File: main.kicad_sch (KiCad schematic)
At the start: 56 parts, among them IC11 BK4802P, IC12 PIC12LF1501-IP, IC14 PIC16F1503-ISL, J11 Conn_01x03, J12 Conn_01x06, J13 Conn_01x03, J14 Conn_01x03, J15 Conn_01x03, J19 Conn_Coaxial, Q11 2N7000, Q12 2N7000, Q13 2N7000, Q14 2N7000, Q15 2N7000, SW11 SW_SPDT, SW12 SW_Push, SW13 SW_Push, U11 LM2936-3.0_TO92, U12 LM2936-3.0, U13 LM2936-3.0, X11 Crystal

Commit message: 部品定数を入力　ただし未評価
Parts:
- C14: value 15p -> 22p
- C19: value 15p -> 27p
- C20: value 10u -> 470u
- C21: value 100p -> 1000p
- C30: value 0.1u -> 1u
- D11: value 1N4002 -> 1N4007
- IC12: value PIC12LF1501-IP -> PIC12F1501-I/P; now left out of the parts list
- IC14: value PIC16F1503-ISL -> PIC16F1503T-I/SL
- R13: value 1k -> 4.7k
- R16: value 1k -> 10
- U11: value LM2936-3.0_TO92 -> LP2950L-33-T92-K; now left out of the parts list
- U12: value LM2936-3.0 -> NJM2391DL1-33
- U13: value LM2936-3.0 -> LM2940T-3.3; now left out of the parts list
- X11: value Crystal -> 21.25M
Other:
- note added: "12Vの場合はレギュレータの放熱に注意 3.3V供給とする場合はU11でジャンパ"
- note added: "BAND"
- note added: "CAUTION: PCB mistake"
- note added: "DC IN"
- note added: "MIC"
- note added: "NM"
- note added: "PICKIT"
- note added: "PICkitからの電源で動かす場合 電源供給は3.3Vなので注意"
- note added: "PTT"
- note added: "R17はカイロミス 本来は3.3Vラインの切り離し用"
- note added: "SOPタイプのPICを使う前提 書き込みはコネクタにPICkitを接続して行う DIPを使う場合はPICkitのコネクタは実装できない"
- note added: "SPK"
- note added: "シリーズに抵抗を入れないと電源が厳しい"
- note added: "スケルチはコマンド制御不可なのでボリュームにすべき"
- note added: "ダイオードスイッチ用"
- note added: "ピン配置を間違えているので改造が必要"
- note added: "ミス：1/6Wパターン"
- note added: "レギュレータは使うたいものを実装 TO-92タイプは消費電流に注意 （スピーカ駆動は不可）"
- note added: "無線部分だけ切り離す場合に使う"
- note added: "逓倍数が大きいので周波数を合わせないと誤差が大きい"
- note added: "電源確認後に実装"
- company: (none) -> JK1MLY / PRUG
- title: (none) -> FM QRP TRCV

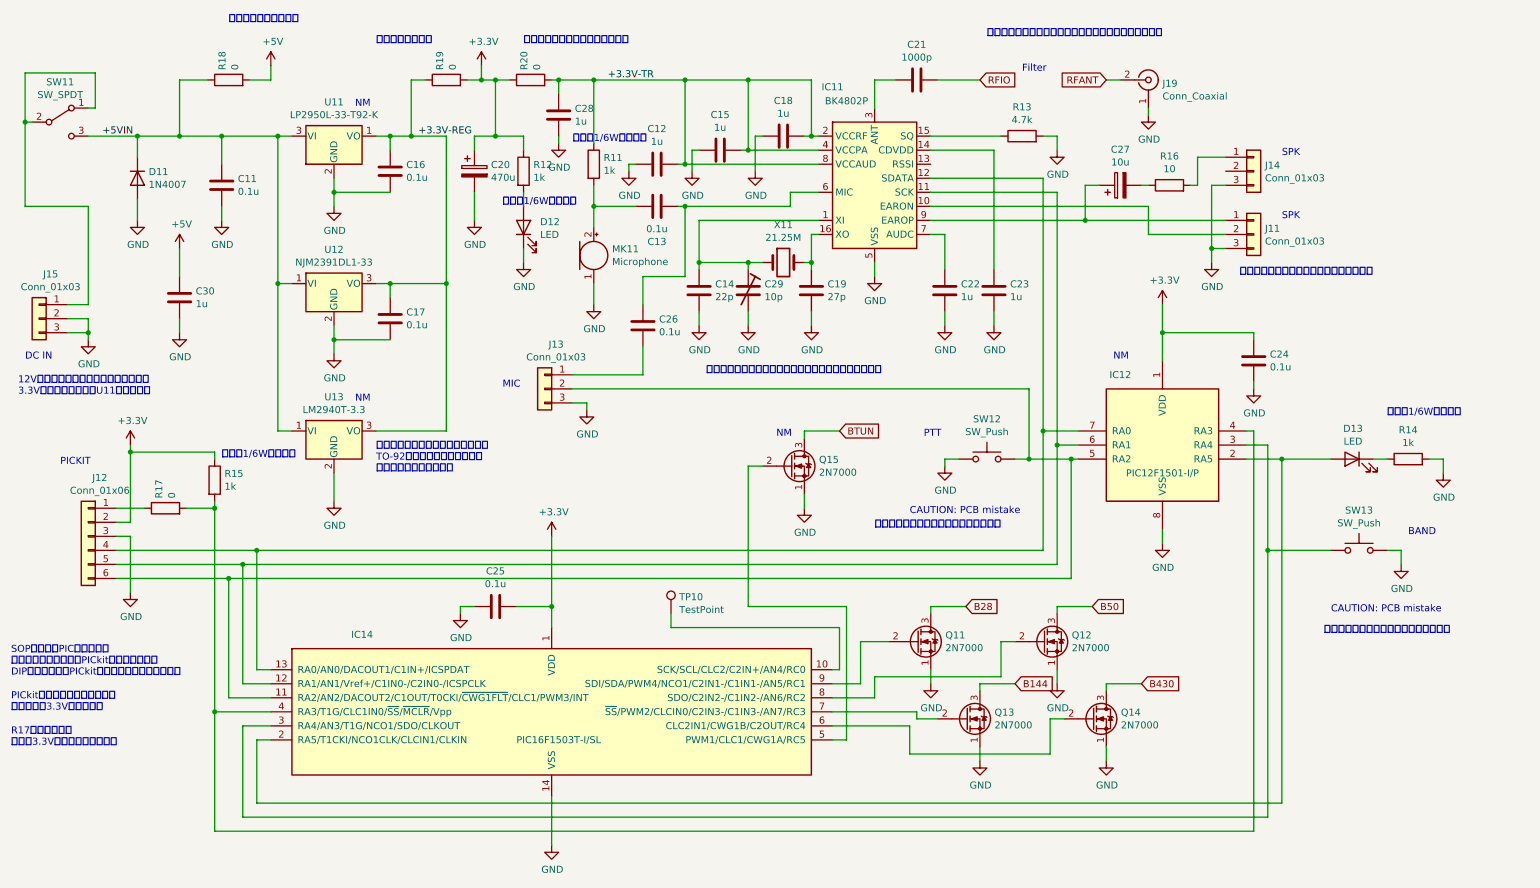
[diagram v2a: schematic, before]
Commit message: Add files via upload
フィルタ回路変更とジャンパクリーン
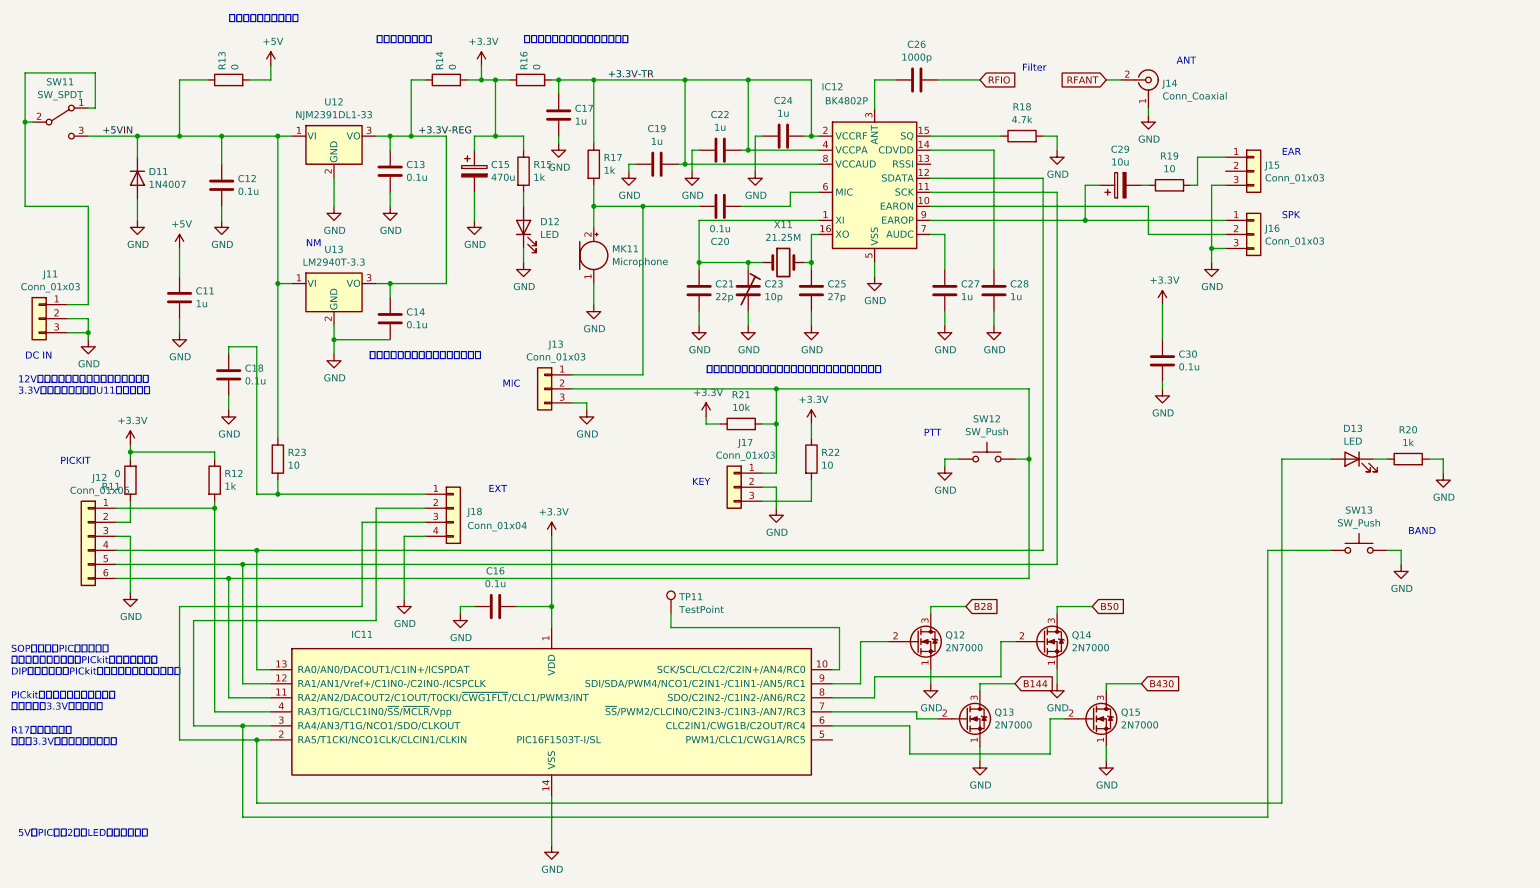
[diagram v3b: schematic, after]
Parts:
- removed C26: 0.1u, Capacitor_THT:C_Disc_D3.4mm_W2.1mm_P2.50mm, symbol Device:C
- removed IC12: PIC12F1501-I/P, digikey-footprints:DIP-8_W7.62mm, symbol MCU_Microchip_PIC12:PIC12LF1501-IP
- removed Q15: 2N7000, Package_TO_SOT_THT:TO-92_Inline_Wide, symbol Transistor_FET:2N7000
- removed U11: LP2950L-33-T92-K, Package_TO_SOT_THT:TO-92_Inline_Wide, symbol Regulator_Linear:LM2936-3.0_TO92
- added C18: 0.1u, Capacitor_THT:C_Disc_D3.4mm_W2.1mm_P2.50mm, symbol Device:C
- added J17: Conn_01x03, Connector_PinHeader_2.54mm:PinHeader_1x03_P2.54mm_Vertical, symbol Connector_Generic:Conn_01x03
- added J18: Conn_01x04, Connector_PinHeader_2.54mm:PinHeader_1x04_P2.54mm_Vertical, symbol Connector_Generic:Conn_01x04
- added R21: 10k, Resistor_THT:R_Axial_DIN0207_L6.3mm_D2.5mm_P2.54mm_Vertical, symbol Device:R
- added R22: 10, Resistor_THT:R_Axial_DIN0207_L6.3mm_D2.5mm_P2.54mm_Vertical, symbol Device:R
- added R23: 10, Resistor_THT:R_Axial_DIN0204_L3.6mm_D1.6mm_P7.62mm_Horizontal, symbol Device:R
- C23: renamed from C29; footprint UserLib:C_TRIM_P6.00mm -> usr-Library:C_TRIM_P6.00mm
- R11: renamed from R17; footprint Resistor_THT:R_Axial_DIN0204_L3.6mm_D1.6mm_P5.08mm_Horizontal -> Resistor_THT:R_Axial_DIN0204_L3.6mm_D1.6mm_P7.62mm_Horizontal
- R12: renamed from R15; footprint Resistor_THT:R_Axial_DIN0204_L3.6mm_D1.6mm_P5.08mm_Horizontal -> Resistor_THT:R_Axial_DIN0204_L3.6mm_D1.6mm_P7.62mm_Horizontal
- R13: renamed from R18; footprint Resistor_THT:R_Axial_DIN0204_L3.6mm_D1.6mm_P5.08mm_Horizontal -> Resistor_THT:R_Axial_DIN0204_L3.6mm_D1.6mm_P7.62mm_Horizontal
- R14: renamed from R19; footprint Resistor_THT:R_Axial_DIN0204_L3.6mm_D1.6mm_P5.08mm_Horizontal -> Resistor_THT:R_Axial_DIN0204_L3.6mm_D1.6mm_P7.62mm_Horizontal
- R15: renamed from R12; footprint Resistor_THT:R_Axial_DIN0204_L3.6mm_D1.6mm_P5.08mm_Horizontal -> Resistor_THT:R_Axial_DIN0204_L3.6mm_D1.6mm_P7.62mm_Horizontal
- R16: renamed from R20; footprint Resistor_THT:R_Axial_DIN0204_L3.6mm_D1.6mm_P5.08mm_Horizontal -> Resistor_THT:R_Axial_DIN0204_L3.6mm_D1.6mm_P7.62mm_Horizontal
- R17: renamed from R11; footprint Resistor_THT:R_Axial_DIN0204_L3.6mm_D1.6mm_P5.08mm_Horizontal -> Resistor_THT:R_Axial_DIN0207_L6.3mm_D2.5mm_P2.54mm_Vertical
- R20: renamed from R14; footprint Resistor_THT:R_Axial_DIN0204_L3.6mm_D1.6mm_P5.08mm_Horizontal -> Resistor_THT:R_Axial_DIN0204_L3.6mm_D1.6mm_P7.62mm_Horizontal
- renumbered C30 to C11, C11 to C12, C16 to C13, C17 to C14, C20 to C15, C25 to C16, C28 to C17, C12 to C19, C13 to C20, C14 to C21, C15 to C22, C18 to C24, C19 to C25, C21 to C26, C22 to C27, C23 to C28, C27 to C29, C24 to C30, IC14 to IC11, IC11 to IC12, J15 to J11, J19 to J14, J14 to J15, J11 to J16, Q11 to Q12, Q12 to Q14, Q14 to Q15, R13 to R18, R16 to R19, TP10 to TP11
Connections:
- net +3V3: now also R11.2, R21.1, R22.1; no longer J12.2 (Pin_2)
- net +5VIN: now also R23.1
- net GND: now also SW12.2, C18.2, J17.2 (Pin_2), J18.4 (Pin_4); no longer SW12.1
- net at IC11.11 (RA2/AN2/DACOUT2/C1OUT/T0CKI/~{CWG1FLT}/CLC1/PWM3/INT), J12.6 (Pin_6), J13.2 (Pin_2): now also SW12.1, J17.1 (Pin_1), R21.2; no longer SW12.2
- net at D13.2 (A), IC11.2 (RA5/T1CKI/NCO1CLK/CLCIN1/CLKIN): now also J18.3 (Pin_3)
- net at IC11.3 (RA4/AN3/T1G/NCO1/SDO/CLKOUT), SW13.1: now also J18.2 (Pin_2)
- net at IC11.4 (RA3/T1G/CLC1IN0/~{SS}/~{MCLR}/Vpp), R12.2: now also J12.1 (Pin_1); no longer R11.2
- net at C20.1, MK11.2 (+), R17.2: now also J13.1 (Pin_1)
- net at R11.1: now also J12.2 (Pin_2); no longer J12.1 (Pin_1)
- new net: C18.1, J18.1 (Pin_1), R23.2
- new net: J17.3 (Pin_3), R22.2
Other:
- note added: "5VとPICから2本でLEDシリアル接続"
- note added: "ANT"
- note added: "EAR"
- note added: "EXT"
- note added: "KEY"
- note added: "レギュレータは使うたいものを実装"
- note removed: "CAUTION: PCB mistake"
- note removed: "シリーズに抵抗を入れないと電源が厳しい"
- note removed: "スケルチはコマンド制御不可なのでボリュームにすべき"
- note removed: "ピン配置を間違えているので改造が必要"
- note removed: "ミス：1/6Wパターン"
- note removed: "レギュレータは使うたいものを実装 TO-92タイプは消費電流に注意 （スピーカ駆動は不可）"
- moved on the sheet: C20, C30, R11, U12, U13

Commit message: アップデート
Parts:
- removed SW11: SW_SPDT, digikey-footprints:Switch_Slide_11.6x4mm_EG1218, symbol Switch:SW_SPDT
- added C11: 470u, Capacitor_THT:CP_Radial_Tantal_D7.0mm_P2.50mm, symbol Device:CP
- added C31, C32: 0.1u, Capacitor_THT:C_Disc_D3.4mm_W2.1mm_P2.50mm, symbol Device:C
- added D14: LED, digikey-footprints:LED_3mm_Radial, symbol Device:LED
- added R24: 1k, Resistor_THT:R_Axial_DIN0207_L6.3mm_D2.5mm_P2.54mm_Vertical, symbol Device:R
- added TP12: TestPoint, Connector_PinHeader_2.54mm:PinHeader_1x01_P2.54mm_Vertical, symbol Connector:TestPoint
- C20: value 0.1u -> 1u
- C22, C24: value 1u -> 0.1u
- C23: value 10p -> 30p
- C26: value 1000p -> 0.01u
- D11: footprint Diode_THT:D_DO-41_SOD81_P10.16mm_Horizontal -> Diode_THT:D_DO-35_SOD27_P7.62mm_Horizontal
- R15, R20: footprint Resistor_THT:R_Axial_DIN0204_L3.6mm_D1.6mm_P7.62mm_Horizontal -> Resistor_THT:R_Axial_DIN0207_L6.3mm_D2.5mm_P2.54mm_Vertical
- R21: footprint Resistor_THT:R_Axial_DIN0207_L6.3mm_D2.5mm_P2.54mm_Vertical -> Resistor_THT:R_Axial_DIN0204_L3.6mm_D1.6mm_P7.62mm_Horizontal
- renumbered C11 to C33, U13 to IC12, U12 to IC13
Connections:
- net +5V: now also C31.1, C32.1
- net +5VIN: now also J11.1 (Pin_1), C11.1
- net GND: now also R20.1, C11.2, C31.2, C32.2, R24.1; no longer R20.2
- net at IC11.3 (RA4/AN3/T1G/NCO1/SDO/CLKOUT), J18.2 (Pin_2), SW13.1: now also D14.2 (A)
- net at IC11.5 (PWM1/CLC1/CWG1A/RC5): now also TP12.1
- net at D13.1 (K): now also R20.2; no longer R20.1
- new net: D14.1 (K), R24.2
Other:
- moved on the sheet: C33, R20
